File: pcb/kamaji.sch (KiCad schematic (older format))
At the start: 8 parts, among them J1 USB_OTG, J2 USB_A, U1 ATMEGA328P-PU

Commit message: some progress on the schematics
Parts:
- added J?: ICSP, symbol CONN_02X03
- added LS?: Speaker, symbol Speaker
- added Q? (x2): TIP120, TO_SOT_Packages_THT:TO-220_Vertical, symbol TIP120
- added R?: 20R, symbol R
- added R? (x2): 220R, symbol R
- J1, J2, J3, J4, J5: renamed from J?; footprint (none) -> kamaji:RJ10
- renumbered J1 to USB_IN1, J2 to USB_OUT1
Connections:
- net GND: now also USB_OUT1.4 (GND), USB_OUT1.5 (Shield), J?.6 (P6), Q?.3 (E)
- net VCC: now also J?.2 (P2), Q?.2 (C), R?.1
- net LAMP: now reaches U1.14 ((PCINT0/CLKO/ICP1)PB0)
- net LAMP: now also R?.2
- net SND: now reaches U1.15 ((PCINT1/OC1A)PB1)
- net SND: now also R?.2
- net at USB_OUT1.1 (VBUS): now also Q?.3 (E)
- new net: LS?.1, R?.2
- new net: LS?.2, Q?.2 (C)
- new net: Q?.1 (B), R?.1 (x2)
- new net MISO: J?.1 (P1)
- new net MOSI: J?.4 (P4)
- new net RST: J?.5 (P5)
- new net SCK: J?.3 (P3)
- no-connect marks 0 -> 5
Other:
- note added: "Buzzer"
- note added: "Player sockets"
- note added: "Power"
- note added: "USB out"
- moved on the sheet: U1, USB_IN1, USB_OUT1

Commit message: first version of the schematic
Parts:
- added C1, C2, C3: 0.1uF, symbol C
- added DS1: LCD-016N002L, WC1602A, symbol LCD-016N002L
- added R1: 10K, symbol R
- added RV1, RV2: POT, symbol POT
- added SW1: CTRL1, symbol SW_Push
- added SW2: CTRL2, symbol SW_Push
- added SW3: CTRL3, symbol SW_Push
- added U2: 74HC595, symbol 74HC595
- R4: renamed from R?; value 220R -> 2.2K
- gave numbers to parts that had none: 6
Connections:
- net labels added: CBTN1, CBTN2, CBTN3, LCD_CLK, LCD_DAT, LCD_EN
- wire segments 59 -> 92
- no-connect marks 5 -> 15
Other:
- note added: "Control buttons"
- note added: "Programming header"
- note added: "USB in"
- note removed: "Power"
- moved on the sheet: J6, LS1, Q1, Q2, R2, R3, R4, USB_IN1, USB_OUT1

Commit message: get rid of the shift register
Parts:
- removed C2: 0.1uF, symbol C
- removed U2: 74HC595, symbol 74HC595
- added R5: 220R, symbol R
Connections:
- net labels added: LCD_D0, LCD_D1, LCD_D2, LCD_D3, LCD_RS
- net labels removed: LCD_CLK, LCD_DAT
- wire segments 92 -> 101
- no-connect marks 15 -> 10
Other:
- note added: "Screen"
- moved on the sheet: C3, DS1, J6, LS1, Q1, Q2, R2, R3, R4, RV1, RV2, USB_IN1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

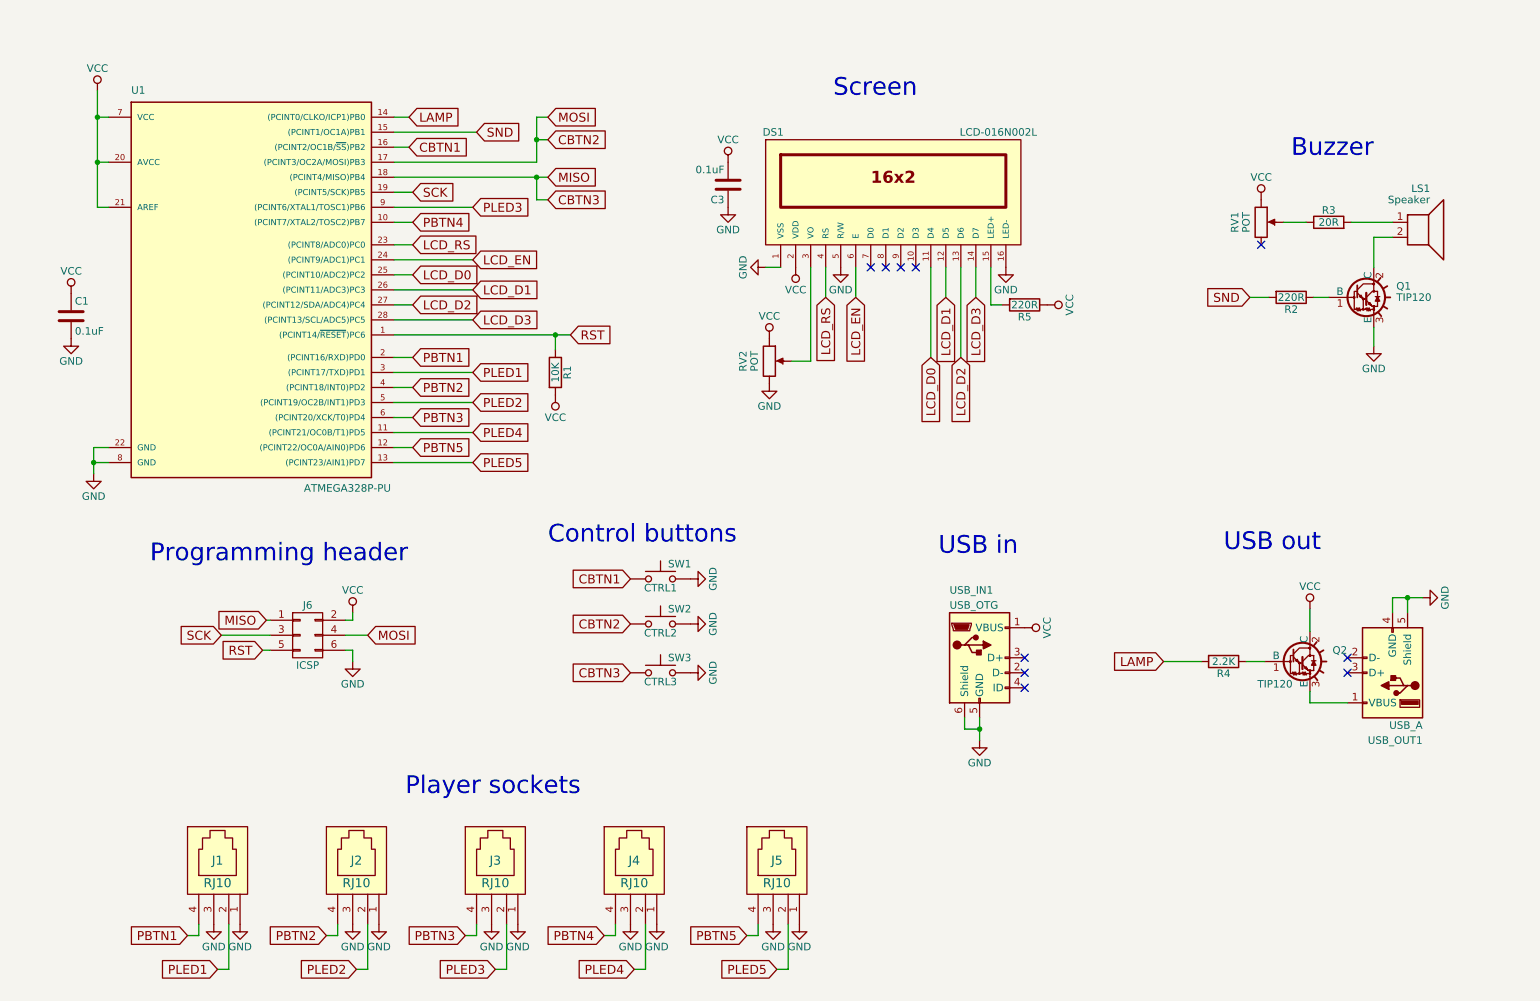
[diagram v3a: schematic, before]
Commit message: add current-limiting resistors for player LEDs
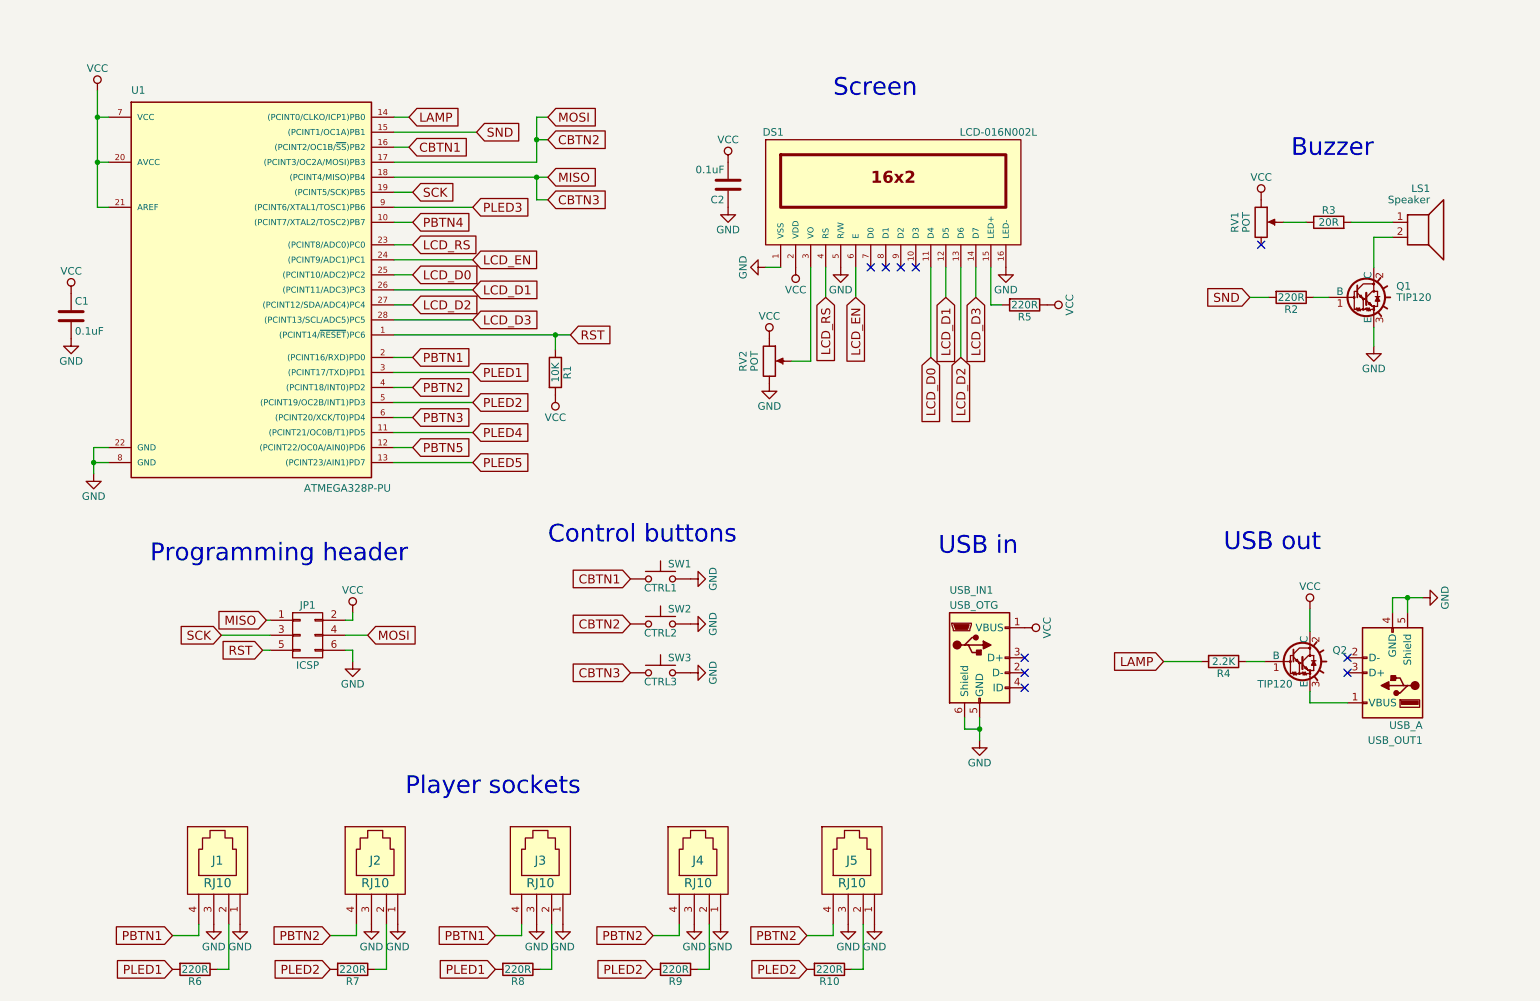
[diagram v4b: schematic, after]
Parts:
- added R10, R6, R7, R8, R9: 220R, symbol R
- renumbered C3 to C2, J6 to JP1
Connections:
- net PBTN1: now also J3.4
- net PBTN2: now also J4.4, J5.4
- net PBTN3: no longer J3.4
- net PBTN4: no longer J4.4
- net PBTN5: no longer J5.4
- net PLED1: now also R6.2, R8.2; no longer J1.2
- net PLED2: now also R10.2, R7.2, R9.2; no longer J2.2
- net PLED3: no longer J3.2
- net PLED4: no longer J4.2
- net PLED5: no longer J5.2
- new net: J1.2, R6.1
- new net: J2.2, R7.1
- new net: J3.2, R8.1
- new net: J4.2, R9.1
- new net: J5.2, R10.1

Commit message: roughly place components on the PCB
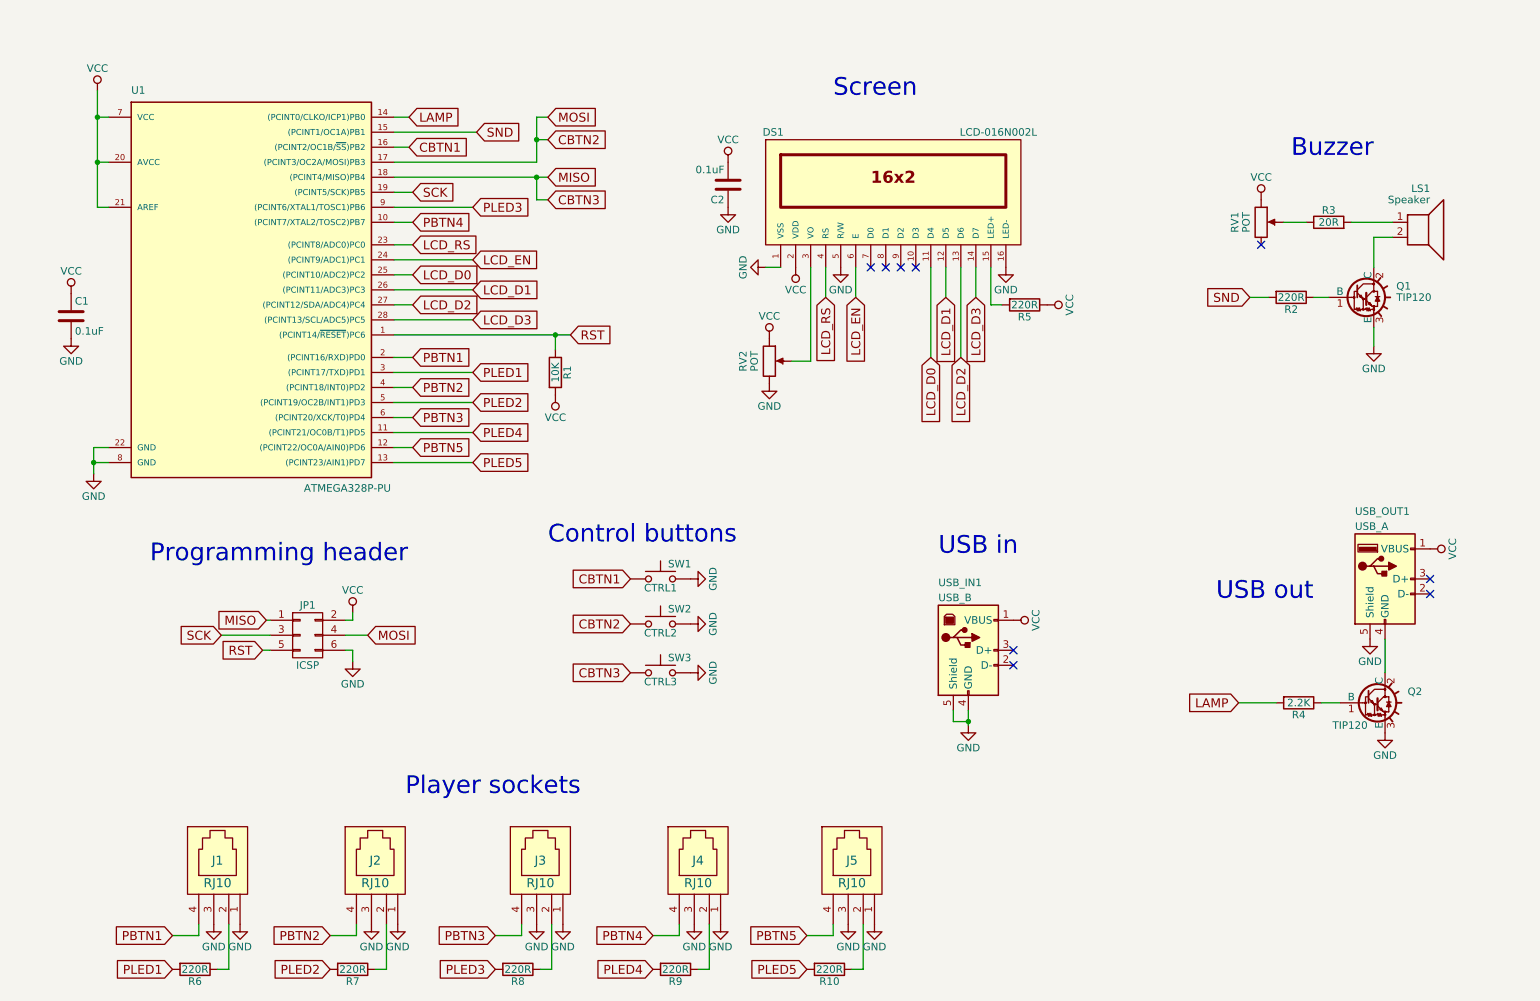
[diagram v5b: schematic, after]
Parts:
- removed USB_IN1: USB_OTG, Connectors:USB_Micro-B, symbol USB_OTG
- added USB_IN1: USB_B, Connectors:USB_B, symbol USB_B
- C1, C2: footprint (none) -> Capacitors_THT:C_Disc_D3.8mm_W2.6mm_P2.50mm
- DS1: footprint WC1602A -> Displays:WC1602A
- JP1: footprint (none) -> Pin_Headers:Pin_Header_Straight_2x03_Pitch2.54mm
- LS1: footprint (none) -> kamaji:AL-30P
- Q1, Q2: footprint TO_SOT_Packages_THT:TO-220_Vertical -> TO_SOT_Packages_THT:TO-220_Horizontal
- R1, R10, R2, R3, R4, R5, R6, R7, R8, R9: footprint (none) -> Resistors_THT:R_Axial_DIN0207_L6.3mm_D2.5mm_P10.16mm_Horizontal
- RV1, RV2: footprint (none) -> Potentiometers:Potentiometer_Triwood_RM-065
- SW1, SW2, SW3: footprint (none) -> Buttons_Switches_THT:SW_PUSH-12mm
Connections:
- net GND: now also Q2.3 (E), USB_IN1.4 (GND), USB_IN1.5 (Shield); no longer USB_OUT1.4 (GND)
- net PBTN1: no longer J3.4
- net PBTN2: no longer J4.4, J5.4
- net PBTN3: now also J3.4
- net PBTN4: now also J4.4
- net PBTN5: now also J5.4
- net PLED1: no longer R8.2
- net PLED2: no longer R10.2, R9.2
- net PLED3: now also R8.2
- net PLED4: now also R9.2
- net PLED5: now also R10.2
- net VCC: now also USB_OUT1.1 (VBUS), USB_IN1.1 (VBUS); no longer Q2.2 (C)
- new net: Q2.2 (C), USB_OUT1.4 (GND)
- no-connect marks 10 -> 9
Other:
- moved on the sheet: Q2, R4, USB_OUT1

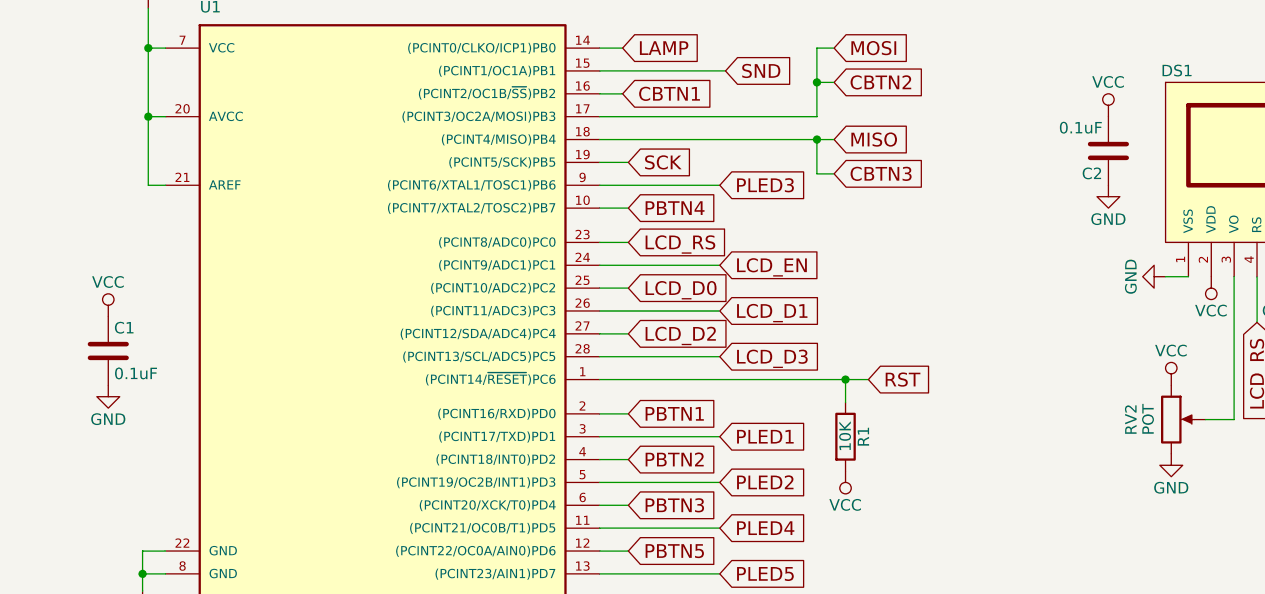
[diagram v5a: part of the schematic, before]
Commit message: minor changes to the schematic
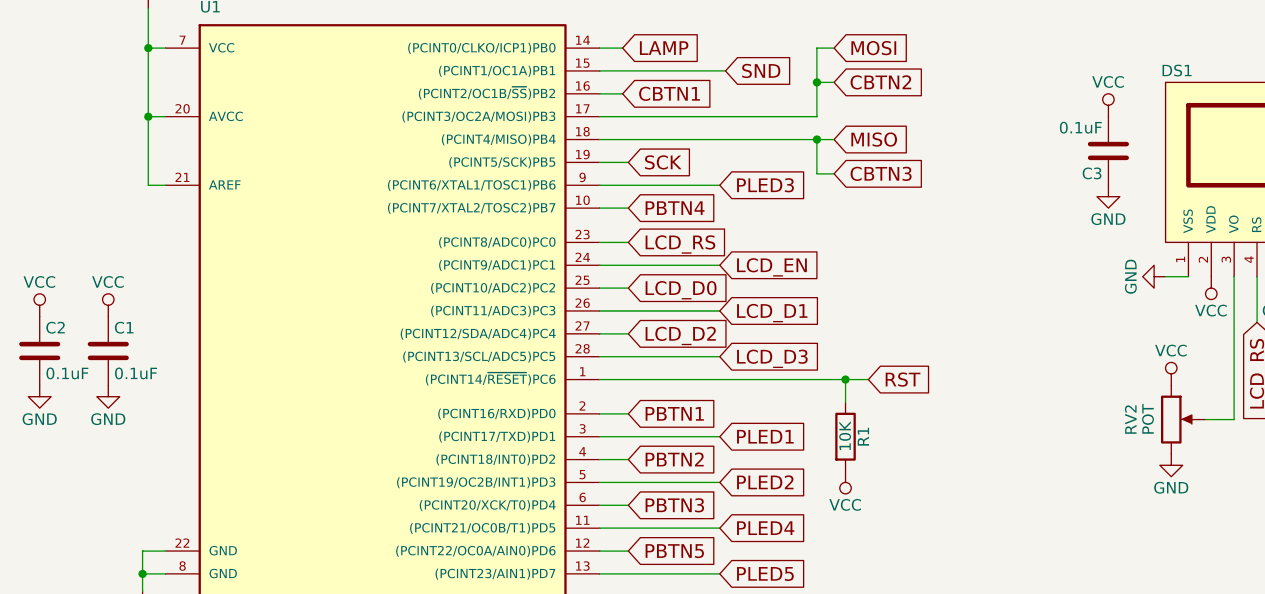
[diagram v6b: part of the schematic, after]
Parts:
- added C2: 0.1uF, Capacitors_THT:C_Disc_D3.8mm_W2.6mm_P2.50mm, symbol C
- JP1: footprint Pin_Headers:Pin_Header_Straight_2x03_Pitch2.54mm -> Connectors:IDC_Header_Straight_6pins
- SW1, SW2, SW3: footprint Buttons_Switches_THT:SW_PUSH-12mm -> Buttons_Switches_THT:SW_PUSH_6mm_h8.5mm
- renumbered C2 to C3
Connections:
- net GND: now also C2.2
- net VCC: now also C2.1
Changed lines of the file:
@@
 Title "Quiz Game System"
 Date ""
-Rev "1.2"
+Rev "1.0"
 Comp "Dead Man's Bluff Inc."
 Comment1 "© Ilya Strukov <iley@iley.ru>"
@@
 F 0 "JP1" H 2575 5200 50  0000 C CNN
 F 1 "ICSP" H 2575 4800 50  0000 C CNN
-F 2 "Pin_Headers:Pin_Header_Straight_2x03_Pitch2.54mm" H 2575 3800 50  0001 C CNN
+F 2 "Connectors:IDC_Header_Straight_6pins" H 2575 3800 50  0001 C CNN
 F 3 "" H 2575 3800 50  0001 C CNN
 	1    2575 5000
@@
 F 0 "SW1" H 4975 4725 50  0000 L CNN
 F 1 "CTRL1" H 4925 4565 50  0000 C CNN
-F 2 "Buttons_Switches_THT:SW_PUSH-12mm" H 4925 4825 50  0001 C CNN
+F 2 "Buttons_Switches_THT:SW_PUSH_6mm_h8.5mm" H 4925 4825 50  0001 C CNN
 F 3 "" H 4925 4825 50  0001 C CNN
 	1    4925 4625
@@
 F 0 "SW2" H 4975 5025 50  0000 L CNN
 F 1 "CTRL2" H 4925 4865 50  0000 C CNN
-F 2 "Buttons_Switches_THT:SW_PUSH-12mm" H 4925 5125 50  0001 C CNN
+F 2 "Buttons_Switches_THT:SW_PUSH_6mm_h8.5mm" H 4925 5125 50  0001 C CNN
 F 3 "" H 4925 5125 50  0001 C CNN
 	1    4925 4925
@@
 F 0 "SW3" H 4975 5350 50  0000 L CNN
 F 1 "CTRL3" H 4925 5190 50  0000 C CNN
-F 2 "Buttons_Switches_THT:SW_PUSH-12mm" H 4925 5450 50  0001 C CNN
+F 2 "Buttons_Switches_THT:SW_PUSH_6mm_h8.5mm" H 4925 5450 50  0001 C CNN
 F 3 "" H 4925 5450 50  0001 C CNN
 	1    4925 5250
@@
 $EndComp
 $Comp
-L C C2
+L C C3
 U 1 1 596C84CE
 P 5375 2000
-F 0 "C2" H 5400 2100 50  0000 L CNN
+F 0 "C3" H 5400 2100 50  0000 L CNN
 F 1 "0.1uF" H 5400 1900 50  0000 L CNN
 F 2 "Capacitors_THT:C_Disc_D3.8mm_W2.6mm_P2.50mm" H 5413 1850 50  0001 C CNN
@@
 	1    0    0    -1
 $EndComp
+$Comp
+L C C2
+U 1 1 5970C40C
+P 700 2875
+F 0 "C2" H 725 2975 50  0000 L CNN
+F 1 "0.1uF" H 725 2775 50  0000 L CNN
+F 2 "Capacitors_THT:C_Disc_D3.8mm_W2.6mm_P2.50mm" H 738 2725 50  0001 C CNN
+F 3 "" H 700 2875 50  0001 C CNN
+	1    700  2875
+	1    0    0    -1
+$EndComp
+$Comp
+L VCC #PWR037
+U 1 1 5970C412
+P 700 2725
+F 0 "#PWR037" H 700 2575 50  0001 C CNN
+F 1 "VCC" H 700 2875 50  0000 C CNN
+F 2 "" H 700 2725 50  0001 C CNN
+F 3 "" H 700 2725 50  0001 C CNN
+	1    700  2725
+	1    0    0    -1
+$EndComp
+$Comp
+L GND #PWR038
+U 1 1 5970C418
+P 700 3025
+F 0 "#PWR038" H 700 2775 50  0001 C CNN
+F 1 "GND" H 700 2875 50  0000 C CNN
+F 2 "" H 700 3025 50  0001 C CNN
+F 3 "" H 700 3025 50  0001 C CNN
+	1    700  3025
+	1    0    0    -1
+$EndComp
